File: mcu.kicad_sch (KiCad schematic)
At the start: 9 parts, among them U1 ATSAMD51J19A-A

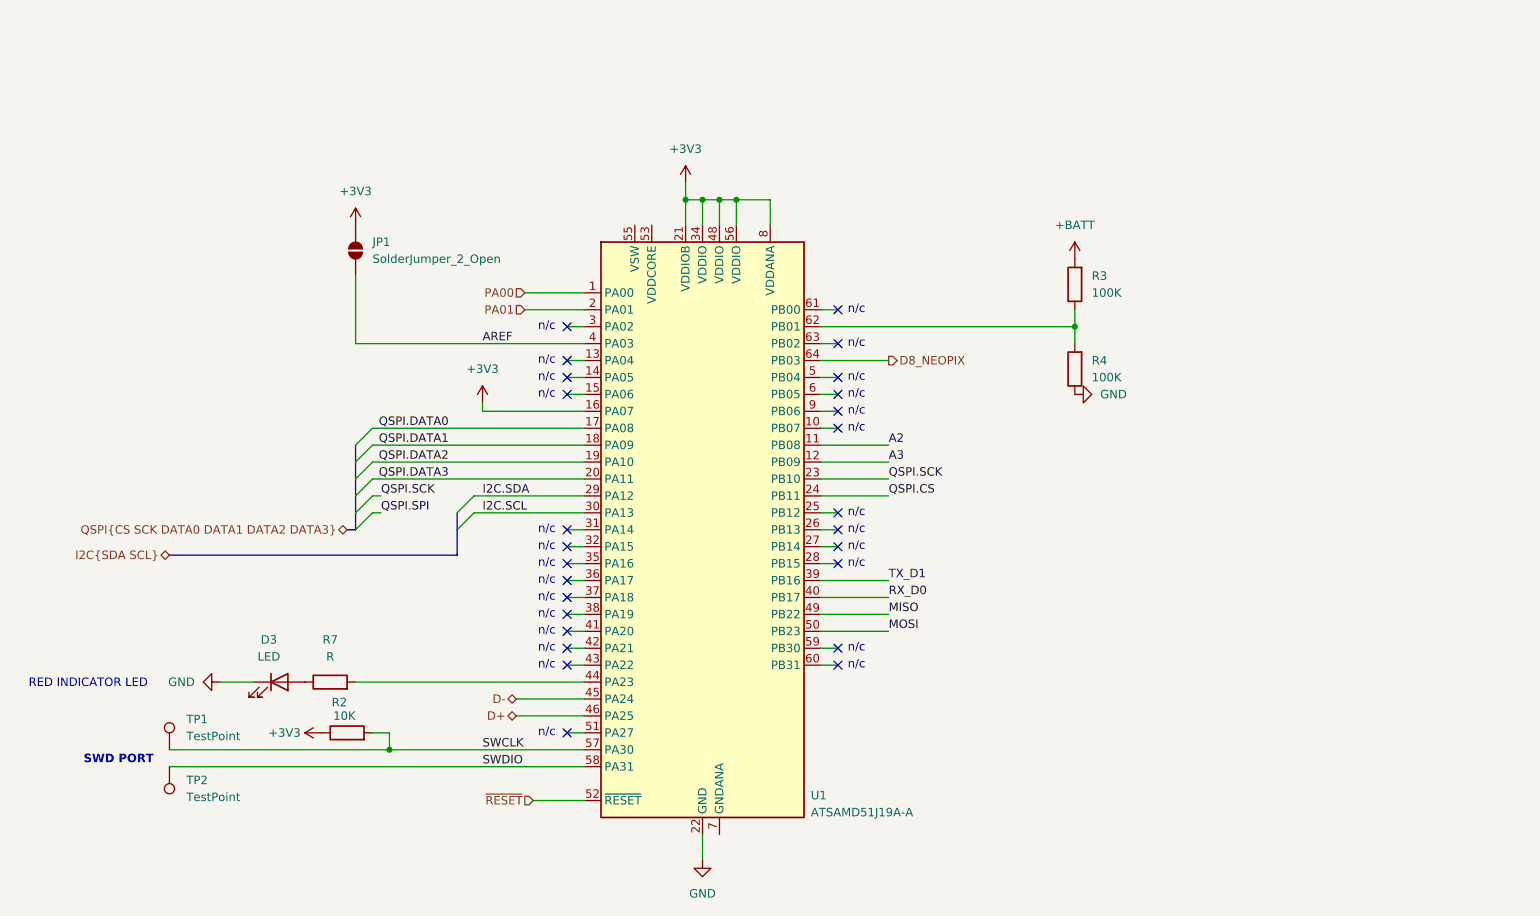
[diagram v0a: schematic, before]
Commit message: Adding symbols information
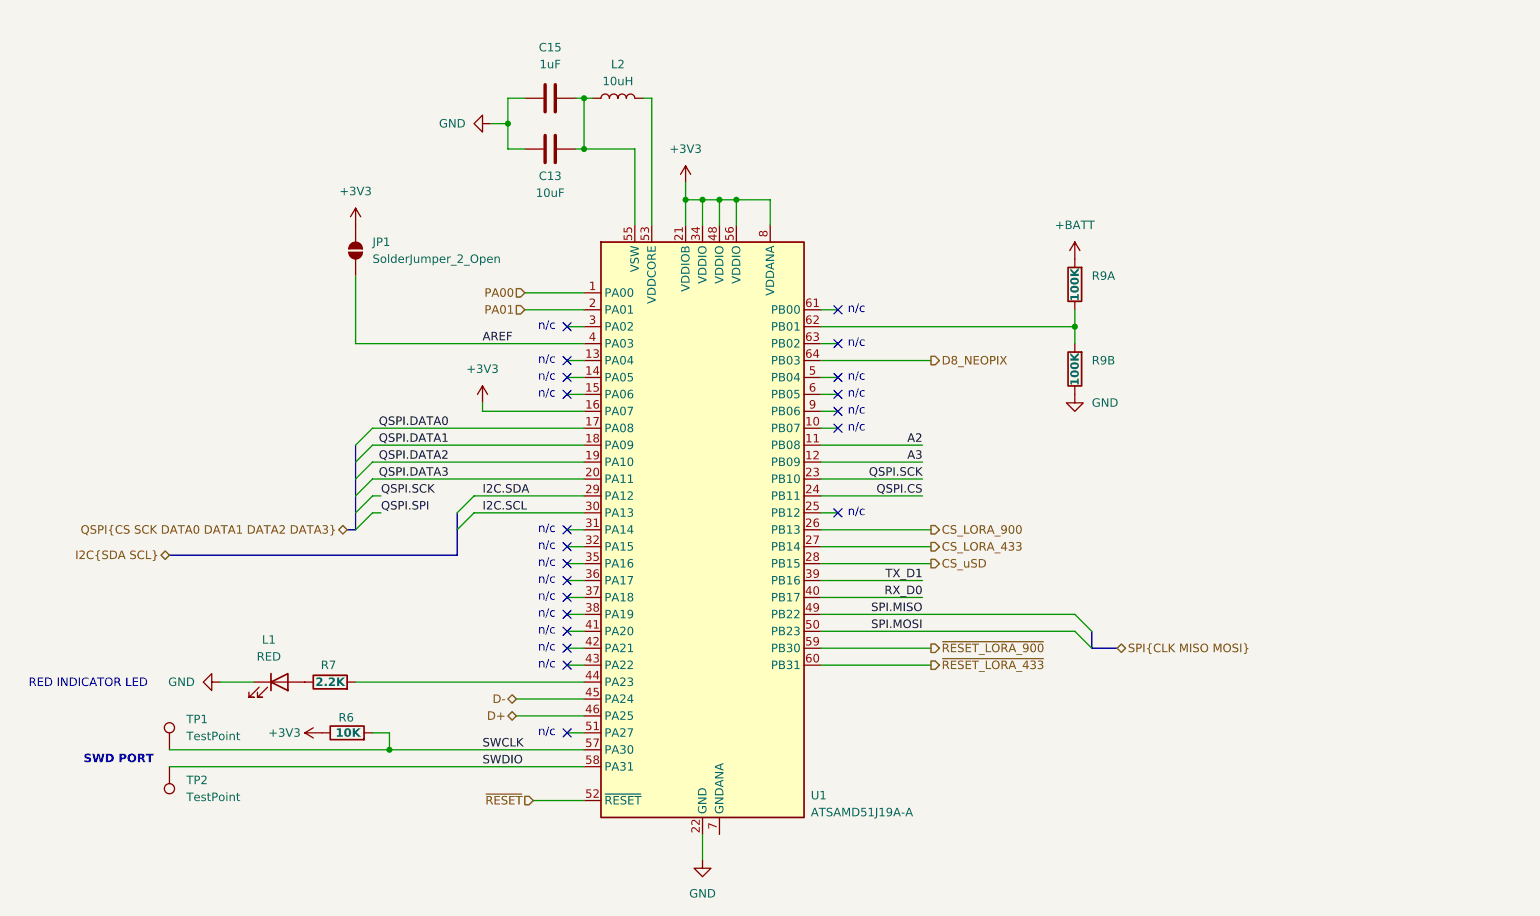
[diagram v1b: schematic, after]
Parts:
- removed R4: 100K, symbol Device:R
- added C13: 10uF, Inductor_SMD:L_0805_2012Metric, symbol Device:C
- added C15: 1uF, Capacitor_SMD:C_0603_1608Metric, symbol Device:C
- added L2: 10uH, Inductor_SMD:L_1008_2520Metric, symbol Device:L
- added R9B: 100K, Resistor_SMD:R_Array_Convex_4x0603, symbol Device:R
- JP1: footprint (none) -> Jumper:SolderJumper-2_P1.3mm_Open_TrianglePad1.0x1.5mm
- L1: renamed from D3; value LED -> RED; footprint (none) -> LED_SMD:LED_0805_2012Metric; Mfr (none) -> Lite-On Inc.; Mfr P/N (none) -> LTST-S220KRKT; Supplier_1 (none) -> Digikey; Supplier_1 P/N (none) -> 160-1469-1-ND; Supplier_1 Price @ Qty (none) -> 0.07620; Supplier_1 Unit Price (none) -> 0.23
- R6: renamed from R2; footprint (none) -> Resistor_SMD:R_0603_1608Metric; Mfr (none) -> Stackpole Electronics Inc; Mfr P/N (none) -> RNCP0603FTD10K0; Supplier_1 (none) -> Digikey; Supplier_1 P/N (none) -> RNCP0603FTD10K0CT-ND; Supplier_1 Price @ Qty (none) -> 0.0170; Supplier_1 Unit Price (none) -> 0.10
- R7: value R -> 2.2K; footprint (none) -> Resistor_SMD:R_0603_1608Metric; Mfr (none) -> TE Connectivity Passive Product; Mfr P/N (none) -> CRGH0603F2K2; Supplier_1 (none) -> Digikey; Supplier_1 P/N (none) -> A129540CT-ND; Supplier_1 Price @ Qty (none) -> 0.01470; Supplier_1 Unit Price (none) -> 0.10
- R9A: renamed from R3; footprint (none) -> Resistor_SMD:R_Array_Convex_4x1206; Mfr (none) -> Bourns Inc.; Mfr P/N (none) -> CAY16-1003F4LF; Supplier_1 (none) -> Digikey; Supplier_1 P/N (none) -> CAY16-1003F4LFCT-ND; Supplier_1 Price @ Qty (none) -> 0.03170; Supplier_1 Unit Price (none) -> 0.10
- U1: Mfr (none) -> Microchip Technology; Mfr P/N (none) -> ATSAMD51J19A-AUTCT-ND; Supplier_1 (none) -> DigiKey; Supplier_1 P/N (none) -> ATSAMD51J19A-AUTCT-ND; Supplier_1 Unit Price (none) -> $5.68
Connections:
- net GND: now also C13.2, C15.1, R9B.1
- net CS_LORA_900: now reaches U1.26 (PB13)
- net CS_LORA_433: now reaches U1.27 (PB14)
- net CS_uSD: now reaches U1.28 (PB15)
- net at U1.53 (VDDCORE): now also L2.2
- net at U1.55 (VSW): now also C13.1, C15.2, L2.1
- net ~{RESET_LORA_900}: now reaches U1.59 (PB30)
- net ~{RESET_LORA_433}: now reaches U1.60 (PB31)
- net at R9A.1, U1.62 (PB01): now also R9B.2
- net MISO renamed SPI.MISO
- net MOSI renamed SPI.MOSI
- no-connect marks 26 -> 21
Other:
- company: (none) -> catbranchman
- title: (none) -> MCU

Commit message: Adding rest of schematic
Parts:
- added C14: 1uF, Capacitor_SMD:C_0603_1608Metric, symbol Device:C
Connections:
- net AREF: now also C14.1
- net GND: now also C14.2
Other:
- moved on the sheet: C13, C15, JP1, L1, L2, R6, R7, R9A, R9B, TP1, TP2, U1

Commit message: Fixing footprint imports
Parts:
- TP1, TP2: footprint (none) -> TestPoint:TestPoint_Pad_D1.5mm
- renumbered U1 to MCU1, R9A to R9A1, R9B to R9B1
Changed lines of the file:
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@@
 			)
 		)
-		(property "Footprint" ""
+		(property "Footprint" "TestPoint:TestPoint_Pad_D1.5mm"
 			(at 78.74 134.62 0)
 			(effects
@@
 		)
 		(property "Description" "test point"
+			(at 73.66 134.62 0)
+			(effects
+				(font
+					(size 1.27 1.27)
+				)
+				(hide yes)
+			)
+		)
+		(property "Mfr" ""
+			(at 73.66 134.62 0)
+			(effects
+				(font
+					(size 1.27 1.27)
+				)
+				(hide yes)
+			)
+		)
+		(property "Mfr P/N" ""
+			(at 73.66 134.62 0)
+			(effects
+				(font
+					(size 1.27 1.27)
+				)
+				(hide yes)
+			)
+		)
+		(property "Supplier_1" ""
+			(at 73.66 134.62 0)
+			(effects
+				(font
+					(size 1.27 1.27)
+				)
+				(hide yes)
+			)
+		)
+		(property "Supplier_1 P/N" ""
+			(at 73.66 134.62 0)
+			(effects
+				(font
+					(size 1.27 1.27)
+				)
+				(hide yes)
+			)
+		)
+		(property "Supplier_1 Unit Price" ""
+			(at 73.66 134.62 0)
+			(effects
+				(font
+					(size 1.27 1.27)
+				)
+				(hide yes)
+			)
+		)
+		(property "Supplier_1 Price @ Qty" ""
+			(at 73.66 134.62 0)
+			(effects
+				(font
+					(size 1.27 1.27)
+				)
+				(hide yes)
+			)
+		)
+		(property "Supplier_2" ""
+			(at 73.66 134.62 0)
+			(effects
+				(font
+					(size 1.27 1.27)
+				)
+				(hide yes)
+			)
+		)
+		(property "Supplier_2 P/N" ""
+			(at 73.66 134.62 0)
+			(effects
+				(font
+					(size 1.27 1.27)
+				)
+				(hide yes)
+			)
+		)
+		(property "Supplier_2 Unit Price" ""
+			(at 73.66 134.62 0)
+			(effects
+				(font
+					(size 1.27 1.27)
+				)
+				(hide yes)
+			)
+		)
+		(property "Supplier_2 Price @ Qty" ""
 			(at 73.66 134.62 0)
 			(effects
@@
 		(on_board yes)
 		(dnp no)
-		(property "Reference" "R9B"
+		(property "Reference" "R9B1"
 			(at 212.09 76.1999 0)
 			(effects
@@
 			(project "roamer"
 				(path "/1c59de6a-87fe-4223-8898-4b0383164a31/8577a42d-e978-4b13-b04c-7762f88202ec"
-					(reference "R9B")
+					(reference "R9B1")
 					(unit 1)
 				)
@@
 		(on_board yes)
 		(dnp no)
-		(property "Reference" "U1"
+		(property "Reference" "MCU1"
 			(at 169.926 141.478 0)
 			(effects
@@
 			(project ""
 				(path "/1c59de6a-87fe-4223-8898-4b0383164a31/8577a42d-e978-4b13-b04c-7762f88202ec"
-					(reference "U1")
+					(reference "MCU1")
 					(unit 1)
 				)
@@
 	)
 	(symbol
+		(lib_id "Connector:TestPoint")
+		(at 73.66 137.16 180)
+		(unit 1)
+		(exclude_from_sim no)
+		(in_bom yes)
+		(on_board yes)
+		(dnp no)
+		(property "Reference" "TP2"
+			(at 76.2 138.684 0)
+			(effects
+				(font
+					(size 1.27 1.27)
+				)
+				(justify right)
+			)
+		)
+		(property "Value" "TestPoint"
+			(at 76.2 141.224 0)
+			(effects
+				(font
+					(size 1.27 1.27)
+				)
+				(justify right)
+			)
+		)
+		(property "Footprint" "TestPoint:TestPoint_Pad_D1.5mm"
+			(at 76.2 143.0019 0)
+			(effects
+				(font
+					(size 1.27 1.27)
+				)
+				(justify right)
+				(hide yes)
+			)
+		)
+		(property "Datasheet" "~"
+			(at 68.58 137.16 0)
+			(effects
+				(font
+					(size 1.27 1.27)
+				)
+				(hide yes)
+			)
+		)
+		(property "Description" "test point"
+			(at 73.66 137.16 0)
+			(effects
+				(font
+					(size 1.27 1.27)
+				)
+				(hide yes)
+			)
+		)
+		(property "Mfr" ""
+			(at 73.66 137.16 0)
+			(effects
+				(font
+					(size 1.27 1.27)
+				)
+				(hide yes)
+			)
+		)
+		(property "Mfr P/N" ""
+			(at 73.66 137.16 0)
+			(effects
+				(font
+					(size 1.27 1.27)
+				)
+				(hide yes)
+			)
+		)
+		(property "Supplier_1" ""
+			(at 73.66 137.16 0)
+			(effects
+				(font
+					(size 1.27 1.27)
+				)
+				(hide yes)
+			)
+		)
+		(property "Supplier_1 P/N" ""
+			(at 73.66 137.16 0)
+			(effects
+				(font
+					(size 1.27 1.27)
+				)
+				(hide yes)
+			)
+		)
+		(property "Supplier_1 Unit Price" ""
+			(at 73.66 137.16 0)
+			(effects
+				(font
+					(size 1.27 1.27)
+				)
+				(hide yes)
+			)
+		)
+		(property "Supplier_1 Price @ Qty" ""
+			(at 73.66 137.16 0)
+			(effects
+				(font
+					(size 1.27 1.27)
+				)
+				(hide yes)
+			)
+		)
+		(property "Supplier_2" ""
+			(at 73.66 137.16 0)
+			(effects
+				(font
+					(size 1.27 1.27)
+				)
+				(hide yes)
+			)
+		)
+		(property "Supplier_2 P/N" ""
+			(at 73.66 137.16 0)
+			(effects
+				(font
+					(size 1.27 1.27)
+				)
+				(hide yes)
+			)
+		)
+		(property "Supplier_2 Unit Price" ""
+			(at 73.66 137.16 0)
+			(effects
+				(font
+					(size 1.27 1.27)
+				)
+				(hide yes)
+			)
+		)
+		(property "Supplier_2 Price @ Qty" ""
+			(at 73.66 137.16 0)
+			(effects
+				(font
+					(size 1.27 1.27)
+				)
+				(hide yes)
+			)
+		)
+		(pin "1"
+		)
+		(instances
+			(project "roamer"
+				(path "/1c59de6a-87fe-4223-8898-4b0383164a31/8577a42d-e978-4b13-b04c-7762f88202ec"
+					(reference "TP2")
+					(unit 1)
+				)
+			)
+		)
+	)
+	(symbol
 		(lib_id "Device:C")
 		(at 95.25 73.66 270)
@@
 	)
 	(symbol
-		(lib_id "Connector:TestPoint")
-		(at 73.66 137.16 180)
-		(unit 1)
-		(exclude_from_sim no)
-		(in_bom yes)
-		(on_board yes)
-		(dnp no)
-		(fields_autoplaced yes)
-		(property "Reference" "TP2"
-			(at 76.2 139.1919 0)
-			(effects
-				(font
-					(size 1.27 1.27)
-				)
-				(justify right)
-			)
-		)
-		(property "Value" "TestPoint"
-			(at 76.2 141.7319 0)
-			(effects
-				(font
-					(size 1.27 1.27)
-				)
-				(justify right)
-			)
-		)
-		(property "Footprint" ""
-			(at 68.58 137.16 0)
-			(effects
-				(font
-					(size 1.27 1.27)
-				)
-				(hide yes)
-			)
-		)
-		(property "Datasheet" "~"
-			(at 68.58 137.16 0)
-			(effects
-				(font
-					(size 1.27 1.27)
-				)
-				(hide yes)
-			)
-		)
-		(property "Description" "test point"
-			(at 73.66 137.16 0)
-			(effects
-				(font
-					(size 1.27 1.27)
-				)
-				(hide yes)
-			)
-		)
-		(pin "1"
-		)
-		(instances
-			(project ""
-				(path "/1c59de6a-87fe-4223-8898-4b0383164a31/8577a42d-e978-4b13-b04c-7762f88202ec"
-					(reference "TP2")
-					(unit 1)
-				)
-			)
-		)
-	)
-	(symbol
 		(lib_id "Device:LED")
 		(at 90.17 124.46 0)
@@
 		(on_board yes)
 		(dnp no)
-		(property "Reference" "R9A"
+		(property "Reference" "R9A1"
 			(at 212.09 63.4999 0)
 			(effects
@@
 			(project ""
 				(path "/1c59de6a-87fe-4223-8898-4b0383164a31/8577a42d-e978-4b13-b04c-7762f88202ec"
-					(reference "R9A")
+					(reference "R9A1")
 					(unit 1)
 				)

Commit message: Spamming 0 ohm resistors
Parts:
- removed R9A1: 100K, Resistor_SMD:R_Array_Convex_4x1206, symbol Device:R
- removed R9B1: 100K, Resistor_SMD:R_Array_Convex_4x0603, symbol Device:R
- added R9: 100K, Resistor_SMD:R_Array_Convex_4x1206, symbol Device:R_Network04_Split
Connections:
- net +BATT: now also R9.1 (R1)
- net GND: now also R9.3 (R2.2)
- net at MCU1.62 (PB01): now also R9.1 (R1), R9.2 (R1.2)

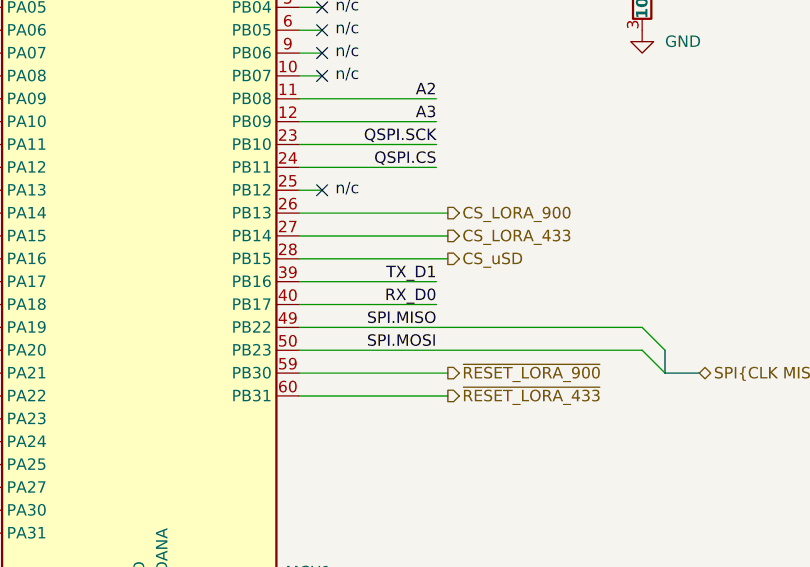
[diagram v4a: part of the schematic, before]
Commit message: Adding diodes for Air Quality Sensor SET and RESET pins
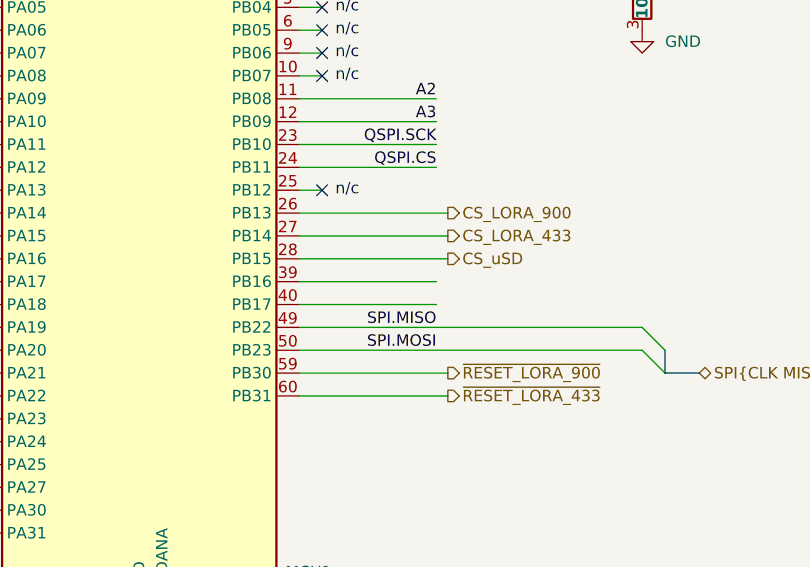
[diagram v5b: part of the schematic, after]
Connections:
- net RX_D0: no longer names the net of MCU1.40 (PB17)
- net TX_D1: no longer names the net of MCU1.39 (PB16)
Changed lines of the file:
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@@
-		)
-	)
-	(label "RX_D0"
-		(at 186.69 111.76 180)
-		(fields_autoplaced yes)
-		(effects
-			(font
-				(size 1.27 1.27)
-			)
-			(justify right bottom)
-		)
-	)
-	(label "TX_D1"
-		(at 186.69 109.22 180)
-		(fields_autoplaced yes)
-		(effects
-			(font
-				(size 1.27 1.27)
-			)
-			(justify right bottom)
 		)
 	)

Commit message: Fixing lots of ERC errors
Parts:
- removed R9: 100K, Resistor_SMD:R_Array_Convex_4x1206, symbol Device:R_Network04_Split
- added R9: 100K, Resistor_THT:R_Array_SIP8, symbol Device:R_Pack04_SIP_Split
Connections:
- net +BATT: now also R9.2 (R1.2)
- net GND: now also MCU1.7 (GNDANA), R9.3 (R2.1)
- net AIRQ_SET: now reaches MCU1.5 (PB04)
- net ~{AIRQ_RESET}: now reaches MCU1.6 (PB05)
- net at MCU1.62 (PB01): now also R9.1 (R1.1), R9.4 (R2.2)
- no-connect marks 21 -> 23
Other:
- moved on the sheet: C13, C15, L2

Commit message: Starting layout
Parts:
- R9: footprint Resistor_THT:R_Array_SIP8 -> Resistor_SMD:R_Array_Convex_4x1206
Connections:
- net AIRQ_SET: now also MCU1.43 (PA22); no longer MCU1.5 (PB04)
- net CS_LORA_433: now also MCU1.35 (PA16); no longer MCU1.27 (PB14)
- net CS_LORA_900: now also MCU1.31 (PA14); no longer MCU1.26 (PB13)
- net CS_uSD: now also MCU1.37 (PA18); no longer MCU1.28 (PB15)
- net ~{AIRQ_RESET}: now also MCU1.42 (PA21); no longer MCU1.6 (PB05)
- net ~{RESET_LORA_433}: now also MCU1.41 (PA20); no longer MCU1.60 (PB31)
- net ~{RESET_LORA_900}: now also MCU1.38 (PA19); no longer MCU1.59 (PB30)
- net SPI.SCK: now reaches MCU1.36 (PA17)
- net A2: no longer names the net of MCU1.11 (PB08)
- net A3: no longer names the net of MCU1.12 (PB09)
- no-connect marks 23 -> 22
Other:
- moved on the sheet: JP1, R7, R9A, R9B, TP1, TP2

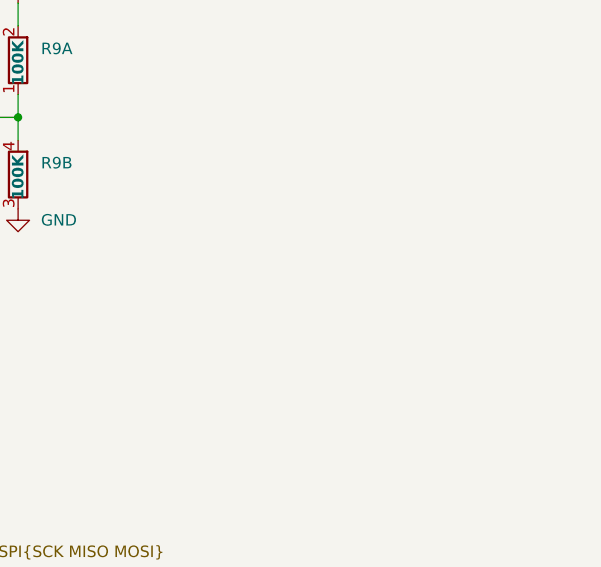
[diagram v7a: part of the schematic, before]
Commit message: Redid board layout. Still have to add bypass caps
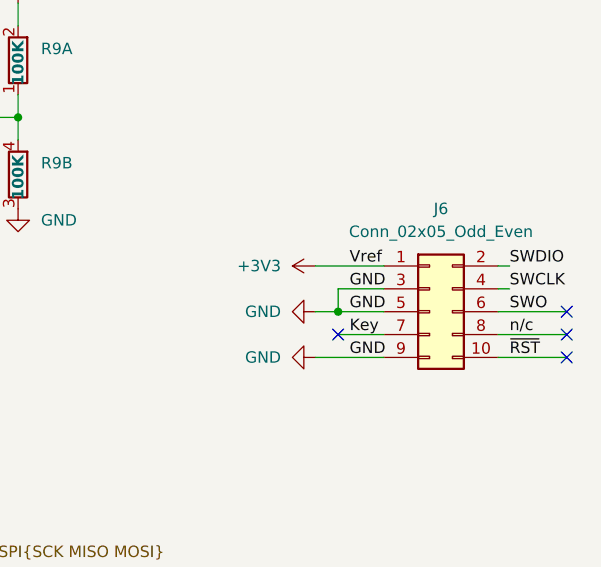
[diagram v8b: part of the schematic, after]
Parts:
- added J6: Conn_02x05_Odd_Even, Connector_PinHeader_1.27mm:PinHeader_2x05_P1.27mm_Vertical_SMD, symbol Connector_Generic:Conn_02x05_Odd_Even
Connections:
- net +3V3: now also J6.1 (Pin_1)
- net GND: now also J6.3 (Pin_3), J6.5 (Pin_5), J6.9 (Pin_9)
- net SWCLK: now also J6.4 (Pin_4)
- net SWDIO: now also J6.2 (Pin_2)
- new net Key: J6.7 (Pin_7)
- new net SWO: J6.6 (Pin_6)
- new net n/c: J6.8 (Pin_8)
- new net ~{RST}: J6.10 (Pin_10)
- no-connect marks 22 -> 26
